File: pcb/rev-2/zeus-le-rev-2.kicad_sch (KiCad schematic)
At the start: 0 parts

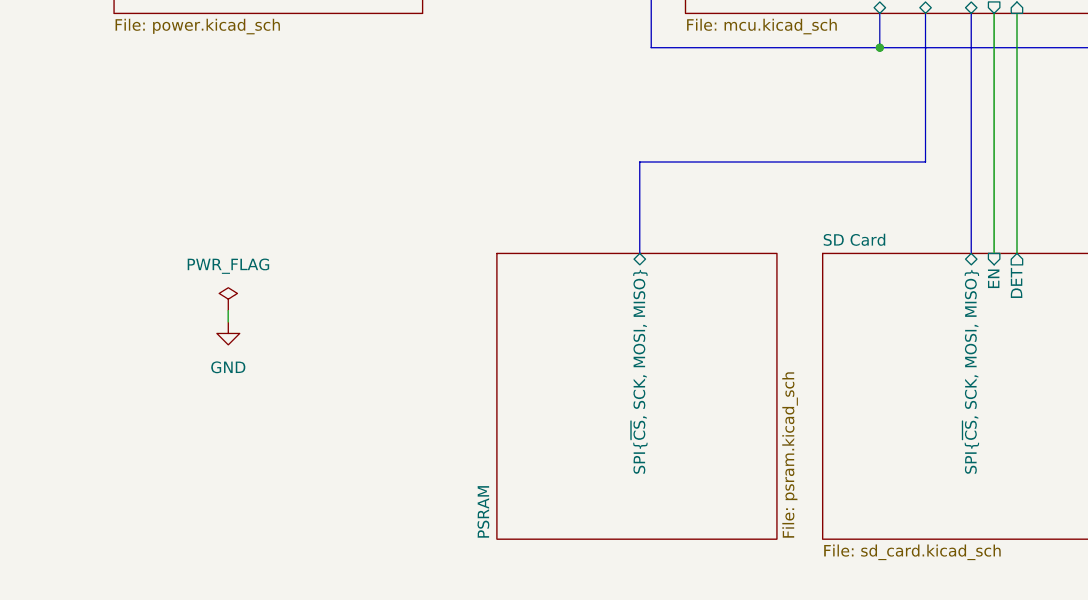
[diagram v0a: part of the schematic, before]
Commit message: pcb: minor schematic cleanup
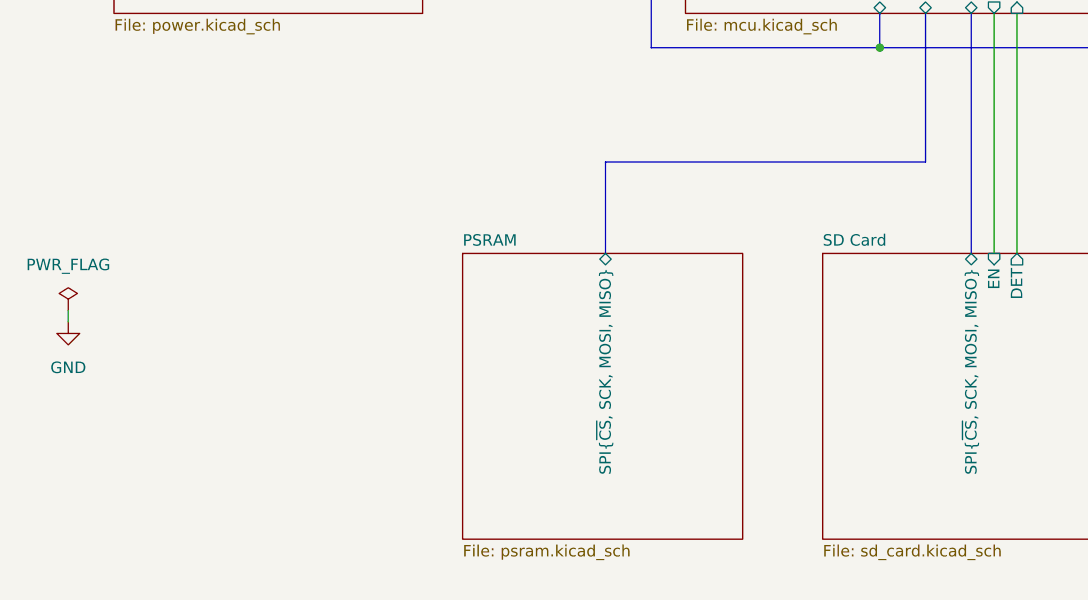
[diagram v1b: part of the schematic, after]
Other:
- title: (none) -> Top Level Design
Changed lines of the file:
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@@
 	(generator_version "8.0")
 	(paper "A4")
+	(title_block
+		(title "Top Level Design")
+		(rev "2")
+	)
 	(junction
 		(at 190.5 80.01)
@@
 	(wire
 		(pts
-			(xy 66.04 116.84) (xy 66.04 115.57)
+			(xy 48.26 116.84) (xy 48.26 115.57)
 		)
 		(stroke
@@
 	(bus
 		(pts
-			(xy 111.76 109.22) (xy 111.76 99.06)
+			(xy 143.51 99.06) (xy 107.95 99.06)
 		)
 		(stroke
@@
 	(bus
 		(pts
+			(xy 107.95 99.06) (xy 107.95 109.22)
+		)
+		(stroke
+			(width 0)
+			(type default)
+		)
+	)
+	(bus
+		(pts
 			(xy 162.56 52.07) (xy 198.12 52.07)
 		)
@@
 		(pts
 			(xy 143.51 99.06) (xy 143.51 82.55)
-		)
-		(stroke
-			(width 0)
-			(type default)
-		)
-	)
-	(bus
-		(pts
-			(xy 111.76 99.06) (xy 143.51 99.06)
 		)
 		(stroke
@@
 	(symbol
 		(lib_id "power:PWR_FLAG")
-		(at 66.04 115.57 0)
+		(at 48.26 115.57 0)
 		(unit 1)
 		(exclude_from_sim no)
@@
 		(fields_autoplaced yes)
 		(property "Reference" "#FLG01"
-			(at 66.04 113.665 0)
+			(at 48.26 113.665 0)
 			(effects
 				(font
@@
 		)
 		(property "Value" "PWR_FLAG"
-			(at 66.04 110.49 0)
+			(at 48.26 110.49 0)
 			(effects
 				(font
@@
 		)
 		(property "Footprint" ""
-			(at 66.04 115.57 0)
+			(at 48.26 115.57 0)
 			(effects
 				(font
@@
 		)
 		(property "Datasheet" "~"
-			(at 66.04 115.57 0)
+			(at 48.26 115.57 0)
 			(effects
 				(font
@@
 		)
 		(property "Description" "Special symbol for telling ERC where power comes from"
-			(at 66.04 115.57 0)
+			(at 48.26 115.57 0)
 			(effects
 				(font
@@
 	(symbol
 		(lib_id "power:GND")
-		(at 66.04 116.84 0)
+		(at 48.26 116.84 0)
 		(unit 1)
 		(exclude_from_sim no)
@@
 		(fields_autoplaced yes)
 		(property "Reference" "#PWR01"
-			(at 66.04 123.19 0)
+			(at 48.26 123.19 0)
 			(effects
 				(font
@@
 		)
 		(property "Value" "GND"
-			(at 66.04 121.92 0)
+			(at 48.26 121.92 0)
 			(effects
 				(font
@@
 		)
 		(property "Footprint" ""
-			(at 66.04 116.84 0)
+			(at 48.26 116.84 0)
 			(effects
 				(font
@@
 		)
 		(property "Datasheet" ""
-			(at 66.04 116.84 0)
+			(at 48.26 116.84 0)
 			(effects
 				(font
@@
 		)
 		(property "Description" "Power symbol creates a global label with name \"GND\" , ground"
-			(at 66.04 116.84 0)
+			(at 48.26 116.84 0)
 			(effects
 				(font
@@
 	)
 	(sheet
-		(at 95.885 109.22)
+		(at 92.075 109.22)
 		(size 31.115 31.75)
 		(fields_autoplaced yes)
@@
 		)
 		(property "Sheetname" "PSRAM"
-			(at 95.1734 140.97 90)
+			(at 92.075 108.5084 0)
 			(effects
 				(font
@@
 		)
 		(property "Sheetfile" "psram.kicad_sch"
-			(at 127.5846 140.97 90)
+			(at 92.075 141.5546 0)
 			(effects
 				(font
@@
 		)
 		(pin "SPI{~{CS}, SCK, MOSI, MISO}" bidirectional
-			(at 111.76 109.22 90)
-			(effects
-				(font
+			(at 107.95 109.22 90)
+			(effects
+				(font
